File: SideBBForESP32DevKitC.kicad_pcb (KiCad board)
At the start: 2 copper layers, 86.4 x 55.9 mm, 8 parts, among them J1 Grove-I2C-connector, J2 mini-bread-board-1x17x2, J3 Grove-I2C-connector, U1 ESP32-DEVKITC-32D

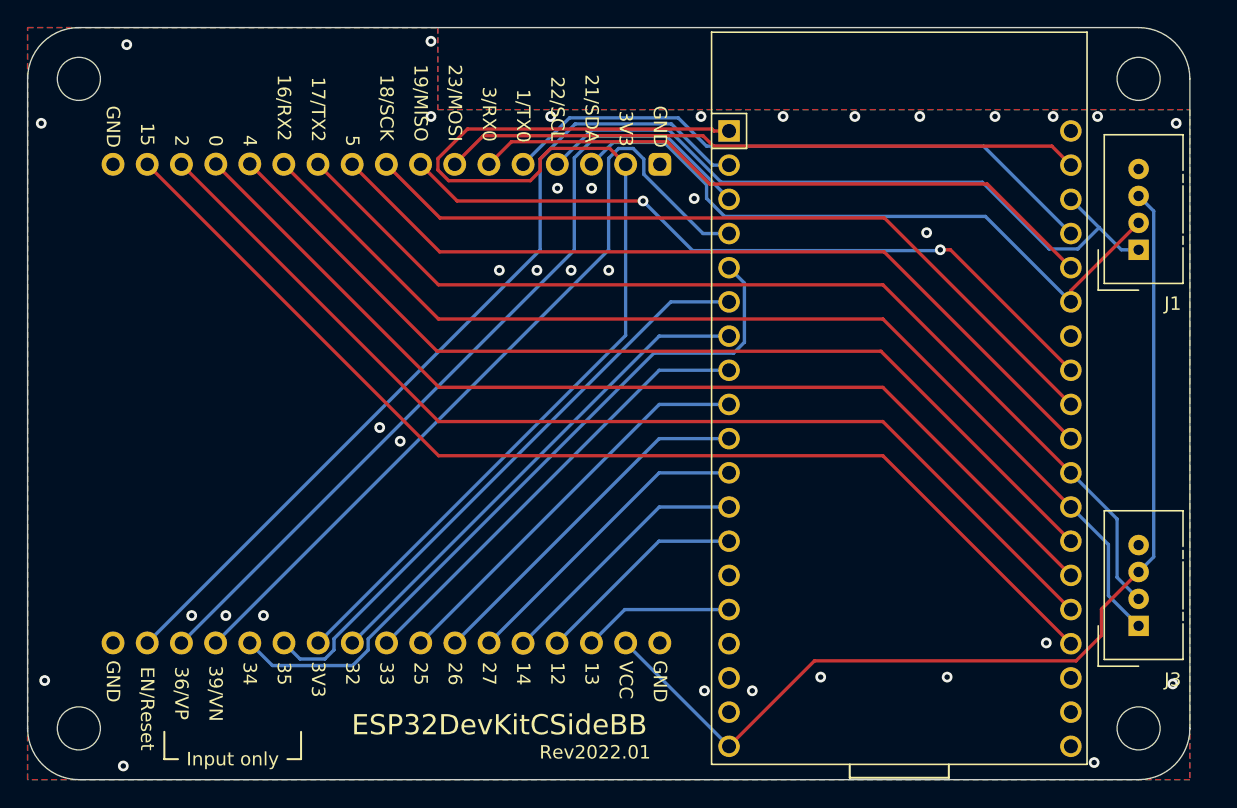
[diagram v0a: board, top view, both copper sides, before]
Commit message: Rename project name to SideBBForESP32DevKitC
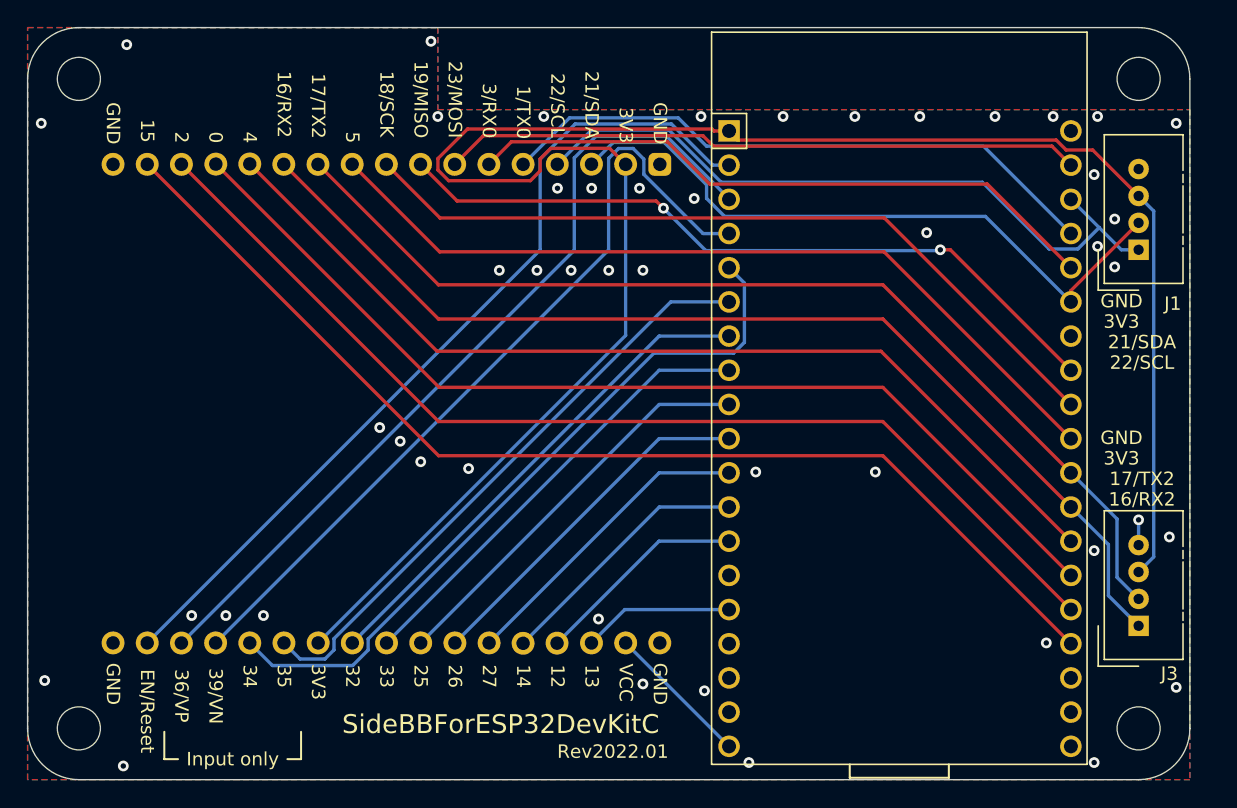
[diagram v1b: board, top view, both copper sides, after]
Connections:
- J1 pad 3: VCC -> +3V3
- J3 pad 3: VCC -> +3V3
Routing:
- net VCC: track 76.7 -> 10.9 mm
- net +3V3: track 84.8 -> 146.1 mm
- net GND: track 0.36 -> 2.24 mm, vias 35 -> 48
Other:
- board text added: "SideBBForESP32DevKitC"
- board text removed: "ESP32DevKitCSideBB"

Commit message: Correct pad for mini bread board
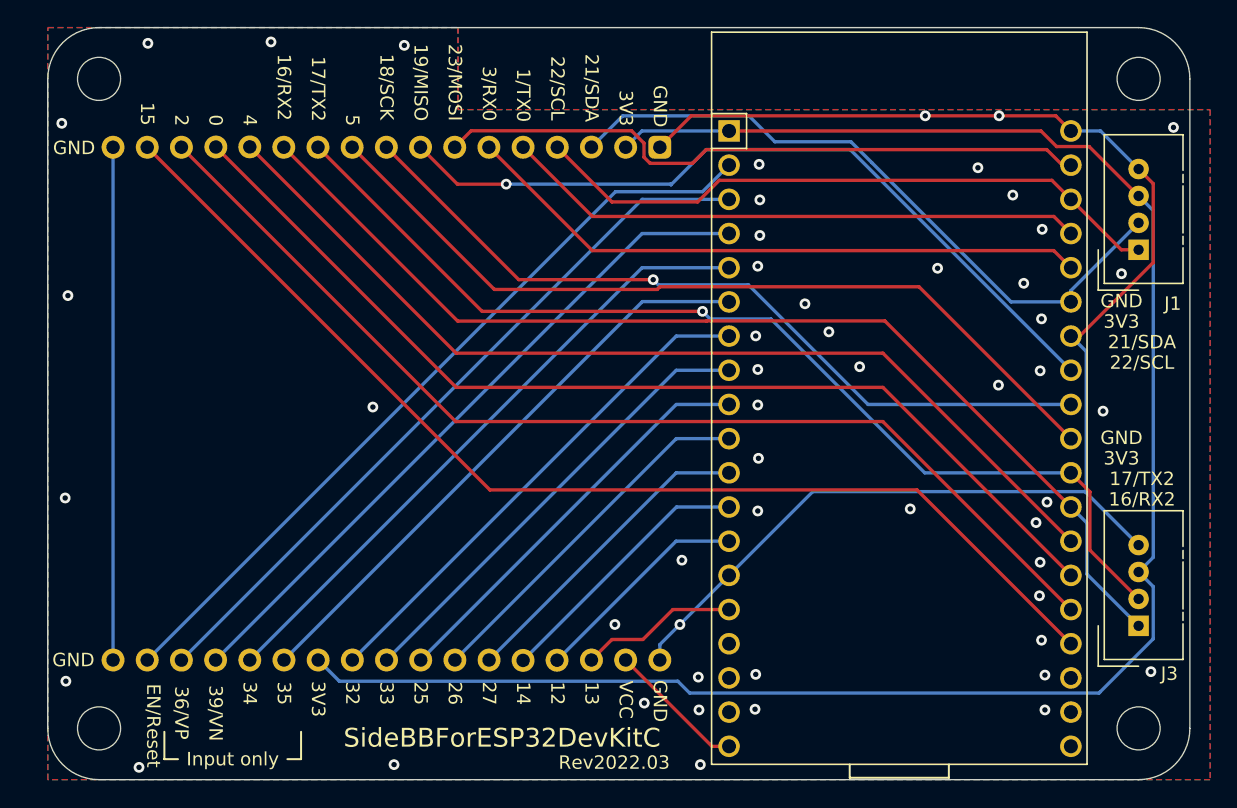
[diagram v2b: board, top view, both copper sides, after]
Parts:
- moved REF3 1.50 mm to (151.4, 100.3)
- moved REF4 1.50 mm to (151.4, 52.1)
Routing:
- net GND: track 2.24 -> 147.2 mm, vias 48 -> 53
- net /39_vn: track 60.6 -> 51.3 mm
- net /36_vp: track 62.3 -> 54.9 mm
- net +3V3: track 146.1 -> 139.6 mm
- net /34: track 53.9 -> 47.7 mm
- net /en_reset: track 64.4 -> 58.5 mm
- net /22_SCL: track 52.2 -> 47.7 mm
- net /19_MISO: track 54.7 -> 57.4 mm, vias 2 -> 1
- net /1_TX0: track 45.7 -> 43.4 mm
- net /23_MOSI: track 47.6 -> 48.8 mm
- net /35: track 45.0 -> 44.1 mm
- net /3_RX0: track 47.8 -> 47.0 mm
- net /5: track 61.8 -> 62.5 mm
- net /16_RX2: track 79.9 -> 80.5 mm
- net /18_SCK: track 58.3 -> 58.8 mm, vias 0 -> 1
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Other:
- board size 86.4 x 55.9 mm -> 84.9 x 55.9 mm
- board text added: "Rev2022.03"
- board text removed: "Rev2022.01"

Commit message: Remove mask for mounting holes and move gnd label position
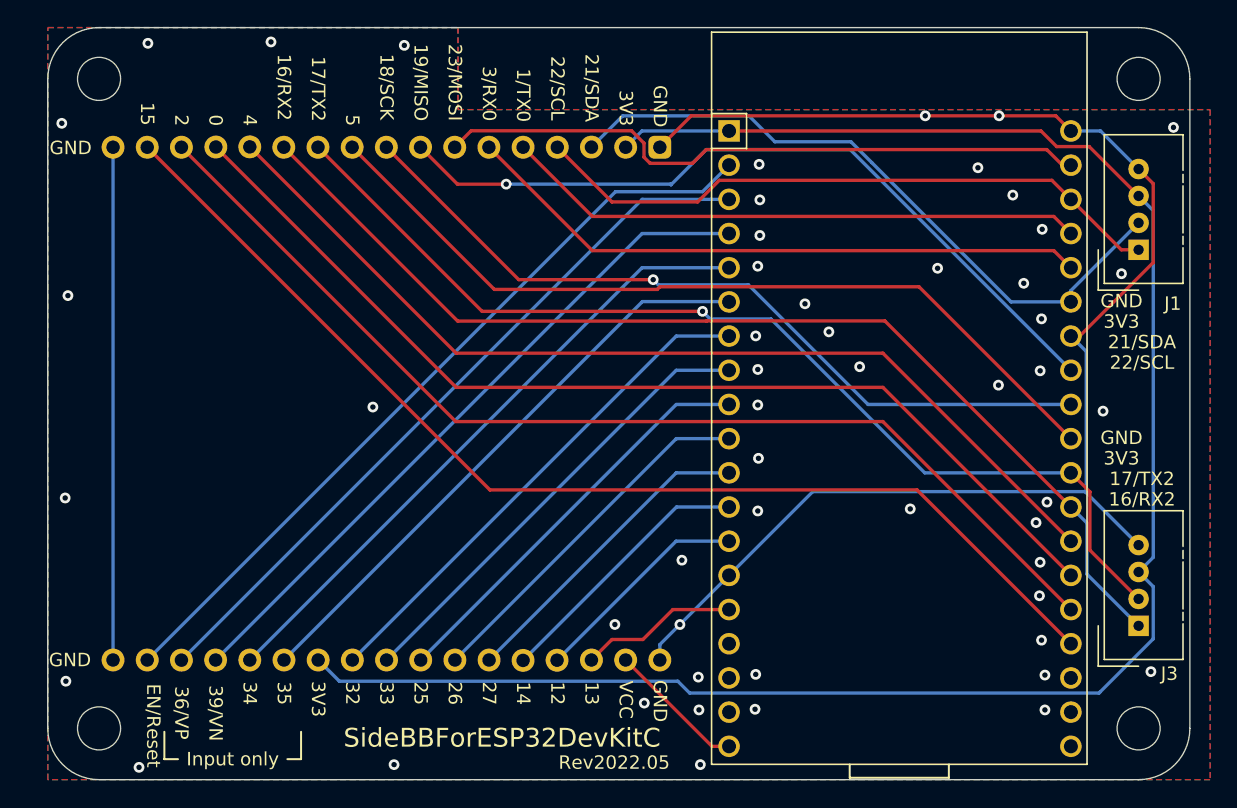
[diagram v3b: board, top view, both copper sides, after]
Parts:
- REF1, REF2, REF3, REF4: value MountingHole_3.2mm_M3 -> MountingHole_3.2mm_M3_bare; footprint MountingHole:MountingHole_3.2mm_M3 -> asukiaaa-kicad-footprints:MountingHole_3.2mm_M3_bare
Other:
- board text added: "Rev2022.05"
- board text added: "https://github.com/asukiaaa/SideBBForESP32DevKitC"
- board text removed: "Rev2022.03"
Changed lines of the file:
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@@
     )
   )
-  (footprint "MountingHole:MountingHole_3.2mm_M3" (layer "F.Cu")
+  (footprint "asukiaaa-kicad-footprints:MountingHole_3.2mm_M3_bare" (layer "F.Cu")
     (at 228.6 100.33)
     (descr "Mounting Hole 3.2mm, no annular, M3")
     (tags "mounting hole 3.2mm no annular m3")
-    (clearance 2)
     (attr exclude_from_pos_files exclude_from_bom)
     (fp_text reference "REF2" (at 0 -4.2) (layer "F.SilkS") hide
       (effects (font (size 1 1) (thickness 0.15)))
     )
-    (fp_text value "MountingHole_3.2mm_M3" (at 0 4.2) (layer "F.Fab") hide
-      (effects (font (size 1 1) (thickness 0.15)))
-    )
-    (fp_text user "${REFERENCE}" (at 0.3 0) (layer "F.Fab")
+    (fp_text value "MountingHole_3.2mm_M3_bare" (at 0 4.2) (layer "F.Fab") hide
+      (effects (font (size 1 1) (thickness 0.15)))
+    )
+    (fp_text user "${REFERENCE}" (at 0 0) (layer "F.Fab")
       (effects (font (size 1 1) (thickness 0.15)))
     )
     (fp_circle (center 0 0) (end 3.2 0) (layer "Cmts.User") (width 0.15) (fill none))
     (fp_circle (center 0 0) (end 3.45 0) (layer "F.CrtYd") (width 0.05) (fill none))
-    (pad "" np_thru_hole circle locked (at 0 0) (size 3.2 3.2) (drill 3.2) (layers *.Cu *.Mask))
-  )
-  (footprint "MountingHole:MountingHole_3.2mm_M3" (layer "F.Cu")
+    (pad "" np_thru_hole circle (at 0 0) (size 3.2 3.2) (drill 3.2) (layers F&B.Cu *.Mask)
+      (solder_mask_margin 1.8) (clearance 2))
+  )
+  (footprint "asukiaaa-kicad-footprints:MountingHole_3.2mm_M3_bare" (layer "F.Cu")
     (at 151.36 52.07)
     (descr "Mounting Hole 3.2mm, no annular, M3")
     (tags "mounting hole 3.2mm no annular m3")
-    (clearance 2)
     (attr exclude_from_pos_files exclude_from_bom)
     (fp_text reference "REF4" (at 0 -4.2) (layer "F.SilkS") hide
       (effects (font (size 1 1) (thickness 0.15)))
     )
-    (fp_text value "MountingHole_3.2mm_M3" (at 0 4.2) (layer "F.Fab") hide
-      (effects (font (size 1 1) (thickness 0.15)))
-    )
-    (fp_text user "${REFERENCE}" (at 0.3 0) (layer "F.Fab")
+    (fp_text value "MountingHole_3.2mm_M3_bare" (at 0 4.2) (layer "F.Fab") hide
+      (effects (font (size 1 1) (thickness 0.15)))
+    )
+    (fp_text user "${REFERENCE}" (at 0 0) (layer "F.Fab")
       (effects (font (size 1 1) (thickness 0.15)))
     )
     (fp_circle (center 0 0) (end 3.2 0) (layer "Cmts.User") (width 0.15) (fill none))
     (fp_circle (center 0 0) (end 3.45 0) (layer "F.CrtYd") (width 0.05) (fill none))
-    (pad "" np_thru_hole circle locked (at 0 0) (size 3.2 3.2) (drill 3.2) (layers *.Cu *.Mask))
-  )
-  (footprint "MountingHole:MountingHole_3.2mm_M3" (layer "F.Cu")
+    (pad "" np_thru_hole circle (at 0 0) (size 3.2 3.2) (drill 3.2) (layers F&B.Cu *.Mask)
+      (solder_mask_margin 1.8) (clearance 2))
+  )
+  (footprint "asukiaaa-kicad-footprints:MountingHole_3.2mm_M3_bare" (layer "F.Cu")
     (at 151.36 100.33)
     (descr "Mounting Hole 3.2mm, no annular, M3")
     (tags "mounting hole 3.2mm no annular m3")
-    (clearance 2)
     (attr exclude_from_pos_files exclude_from_bom)
     (fp_text reference "REF3" (at 0 -4.2) (layer "F.SilkS") hide
       (effects (font (size 1 1) (thickness 0.15)))
     )
-    (fp_text value "MountingHole_3.2mm_M3" (at 0 4.2) (layer "F.Fab") hide
-      (effects (font (size 1 1) (thickness 0.15)))
-    )
-    (fp_text user "${REFERENCE}" (at 0.3 0) (layer "F.Fab")
+    (fp_text value "MountingHole_3.2mm_M3_bare" (at 0 4.2) (layer "F.Fab") hide
+      (effects (font (size 1 1) (thickness 0.15)))
+    )
+    (fp_text user "${REFERENCE}" (at 0 0) (layer "F.Fab")
       (effects (font (size 1 1) (thickness 0.15)))
     )
     (fp_circle (center 0 0) (end 3.2 0) (layer "Cmts.User") (width 0.15) (fill none))
     (fp_circle (center 0 0) (end 3.45 0) (layer "F.CrtYd") (width 0.05) (fill none))
-    (pad "" np_thru_hole circle locked (at 0 0) (size 3.2 3.2) (drill 3.2) (layers *.Cu *.Mask))
+    (pad "" np_thru_hole circle (at 0 0) (size 3.2 3.2) (drill 3.2) (layers F&B.Cu *.Mask)
+      (solder_mask_margin 1.8) (clearance 2))
   )
   (footprint "Connector:NS-Tech_Grove_1x04_P2mm_Vertical" (layer "F.Cu")
@@
       (net 4 "GND") (pinfunction "Pin_34") (pintype "passive"))
   )
-  (footprint "MountingHole:MountingHole_3.2mm_M3" (layer "F.Cu")
+  (footprint "asukiaaa-kicad-footprints:MountingHole_3.2mm_M3_bare" (layer "F.Cu")
     (at 228.6 52.07)
     (descr "Mounting Hole 3.2mm, no annular, M3")
     (tags "mounting hole 3.2mm no annular m3")
-    (clearance 2)
     (attr exclude_from_pos_files exclude_from_bom)
     (fp_text reference "REF1" (at 0 -4.2) (layer "F.SilkS") hide
       (effects (font (size 1 1) (thickness 0.15)))
     )
-    (fp_text value "MountingHole_3.2mm_M3" (at 0 4.2) (layer "F.Fab") hide
-      (effects (font (size 1 1) (thickness 0.15)))
-    )
-    (fp_text user "${REFERENCE}" (at 0.3 0) (layer "F.Fab")
+    (fp_text value "MountingHole_3.2mm_M3_bare" (at 0 4.2) (layer "F.Fab") hide
+      (effects (font (size 1 1) (thickness 0.15)))
+    )
+    (fp_text user "${REFERENCE}" (at 0 0) (layer "F.Fab")
       (effects (font (size 1 1) (thickness 0.15)))
     )
     (fp_circle (center 0 0) (end 3.2 0) (layer "Cmts.User") (width 0.15) (fill none))
     (fp_circle (center 0 0) (end 3.45 0) (layer "F.CrtYd") (width 0.05) (fill none))
-    (pad "" np_thru_hole circle locked (at 0 0) (size 3.2 3.2) (drill 3.2) (layers *.Cu *.Mask))
+    (pad "" np_thru_hole circle (at 0 0) (size 3.2 3.2) (drill 3.2) (layers F&B.Cu *.Mask)
+      (solder_mask_margin 1.8) (clearance 2))
   )
   (gr_line (start 156.21 102.616) (end 157.226 102.616) (layer "F.SilkS") (width 0.15))
@@
   (gr_arc (start 151.360001 104.139999) (mid 148.665924 103.024076) (end 147.550001 100.329999) (layer "Edge.Cuts") (width 0.1))
   (gr_arc (start 228.6 48.26) (mid 231.294077 49.375923) (end 232.41 52.07) (layer "Edge.Cuts") (width 0.1))
+  (gr_text "https://github.com/asukiaaa/SideBBForESP32DevKitC" (at 172.8724 90.5256) (layer "B.SilkS")
+    (effects (font (size 1 1) (thickness 0.2)) (justify mirror))
+  )
   (gr_text "25" (at 175.26 97.726572 270) (layer "F.SilkS")
     (effects (font (size 1 1) (thickness 0.15)))
@@
     (effects (font (size 1 1) (thickness 0.15)))
   )
-  (gr_text "Rev2022.03" (at 189.6364 102.87) (layer "F.SilkS")
+  (gr_text "Rev2022.05" (at 189.6364 102.87) (layer "F.SilkS")
     (effects (font (size 1 1) (thickness 0.15)))
   )
@@
     (effects (font (size 1 1) (thickness 0.15)))
   )
-  (gr_text "GND" (at 149.4536 95.25) (layer "F.SilkS")
+  (gr_text "GND" (at 149.1996 95.25) (layer "F.SilkS")
     (effects (font (size 1 1) (thickness 0.15)))
   )
@@
     (effects (font (size 1 1) (thickness 0.15)))
   )
-  (gr_text "GND" (at 149.5044 57.2008) (layer "F.SilkS")
-    (effects (font (size 1 1) (thickness 0.15)))
-  )
+  (gr_text "GND" (at 149.2504 57.2008) (layer "F.SilkS")
+    (effects (font (size 1 1) (thickness 0.15)))
+  )
